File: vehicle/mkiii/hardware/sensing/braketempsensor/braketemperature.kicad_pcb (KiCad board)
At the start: 2 copper layers, 8.4 x 20.3 mm, 15 parts, among them J1 J_PCIe_x1, J2 J_Programming_Pin_Header, U1 MCP2561-E_SN, U2 STM32G441KBT6, Y1 X_16MHz_18pF

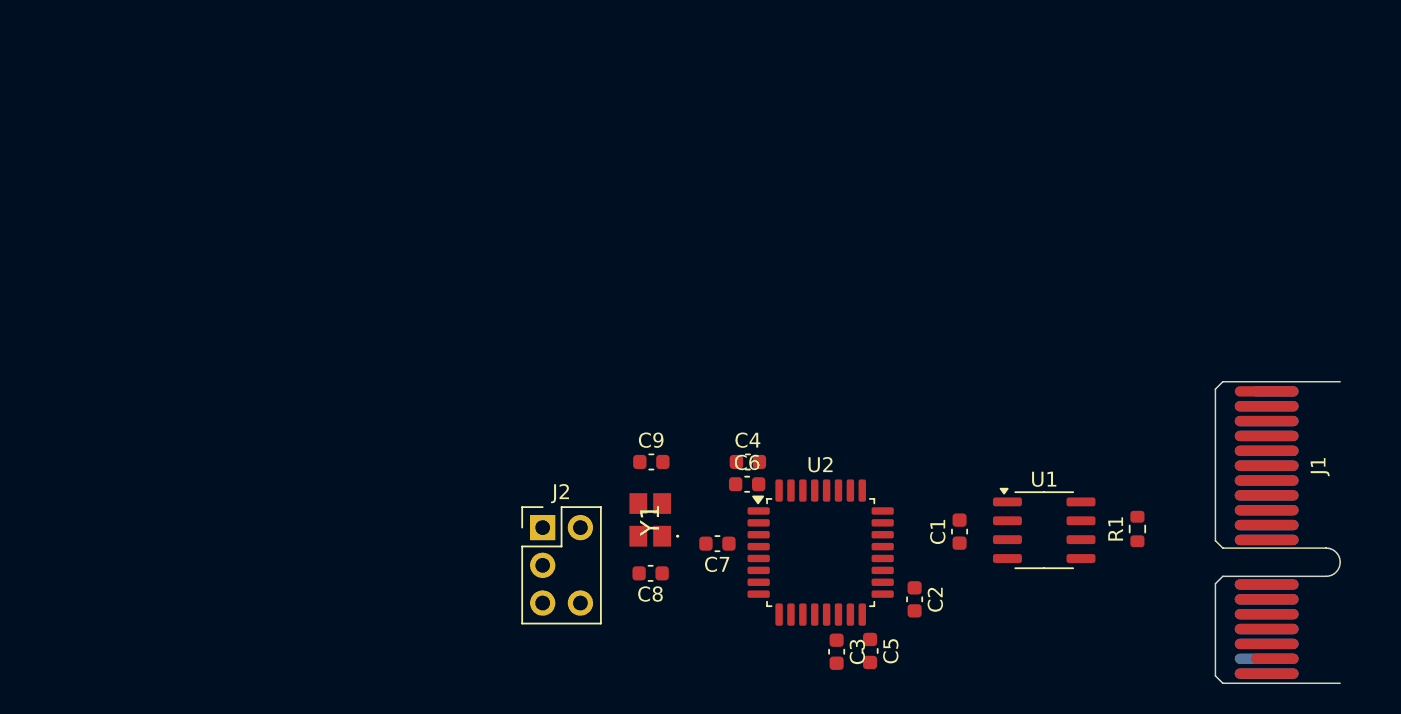
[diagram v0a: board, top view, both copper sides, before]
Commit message: first final draft of brake temp sensor, schematic and pcb layout first completion
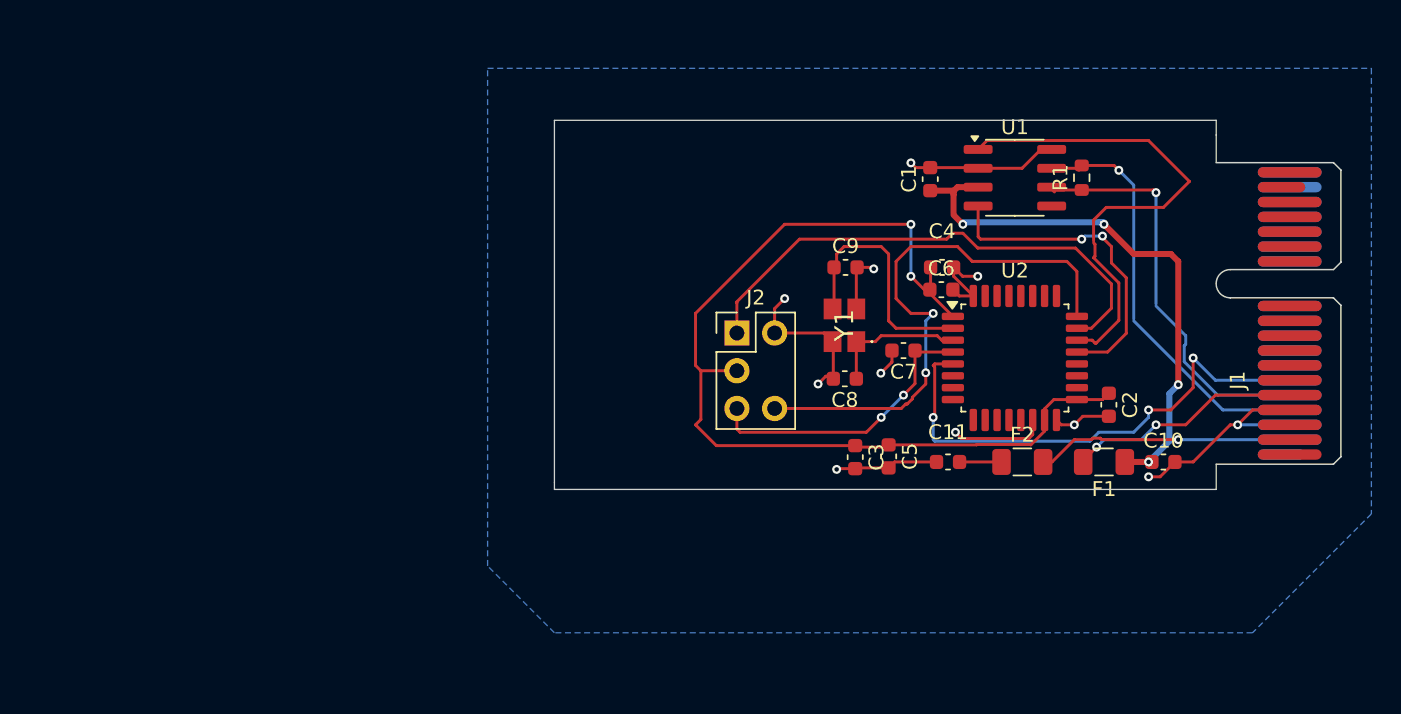
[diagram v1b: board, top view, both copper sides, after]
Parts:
- added C10: C_10uF_10V, OEM:C_0603_1608Metric, F.Cu at (270.0, 42.0)
- added C11: C_10uF_10V, OEM:C_0603_1608Metric, F.Cu at (255.5, 42.0)
- added F1: F_500mA_8V, OEM:Fuse_1206_3216Metric, F.Cu at (266.0, 42.0)
- added F2: F_500mA_8V, OEM:Fuse_1206_3216Metric, F.Cu at (260.5, 42.0)
- moved R1 23.9 mm to (264.5, 22.9)
- moved U1 23.8 mm to (260.0, 22.9)
- moved C1 23.8 mm to (254.3, 23.0)
- moved C6 18.5 mm to (255.1, 30.4)
- moved C8 18.5 mm to (248.6, 36.4)
- moved Y1 18.5 mm to (248.5, 32.8)
- moved C2 18.5 mm to (266.3, 38.1)
- moved C4 18.5 mm to (255.1, 28.9)
- moved C9 18.5 mm to (248.6, 28.9)
- moved J2 18.5 mm to (241.3, 33.3)
- moved U2 18.5 mm to (260.0, 35.0)
- moved C7 18.1 mm to (252.5, 34.5)
- moved C3 13.2 mm to (249.2, 41.7)
- moved C5 13.2 mm to (251.5, 41.6)
- moved J1 4.52 mm to (278.5, 41.5), turned to 90 degrees
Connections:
- J1 pad A2: +3.3V -> Net-(J1-3.3V)
- J1 pad B5: +5V -> Net-(J1-5V)
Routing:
- net +3V3: track 0.00 -> 67.2 mm, vias 0 -> 2
- net GND: track 0.00 -> 64.8 mm, vias 0 -> 11
- net +5V: track 0.00 -> 37.9 mm, vias 0 -> 4
- net /SWCLK: track 0.00 -> 37.6 mm, vias 0 -> 2
- net /SWDIO: track 0.00 -> 35.2 mm
- net /IR Output - PA0: track 0.00 -> 34.9 mm, vias 0 -> 3
- net /CAN_TX: track 0.00 -> 34.1 mm
- net Net-(J1-CAN+): track 0.00 -> 28.1 mm, vias 0 -> 1
- net Net-(J1-CAN-): track 0.00 -> 27.3 mm, vias 0 -> 1
- net /CAN_RX: track 0.00 -> 21.7 mm, vias 0 -> 2
- net /NRST: track 0.00 -> 19.7 mm, vias 0 -> 2
- net Net-(J1-3.3V): track 0.00 -> 17.3 mm, vias 0 -> 1
- net Net-(U2-PF0-OSC_IN): track 0.00 -> 16.5 mm
- net Net-(J1-5V): track 0.00 -> 16.3 mm, vias 0 -> 2
- net Net-(U2-PF1-OSC_OUT): track 0.00 -> 9.43 mm
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- added copper zone on B.Cu, net GND
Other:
- board size 8.4 x 20.3 mm -> 44.6 x 24.9 mm

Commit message: Fixed Vias DRC Issues by changing project to OEM Template
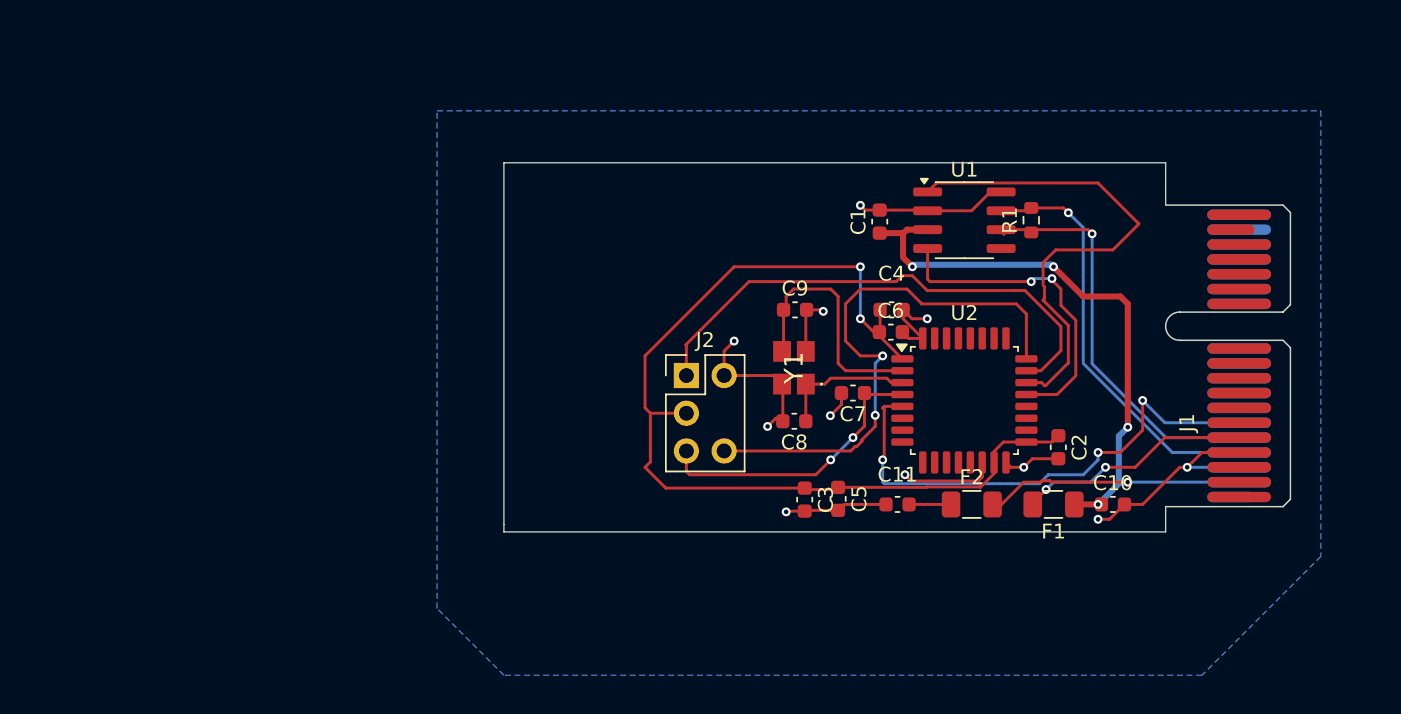
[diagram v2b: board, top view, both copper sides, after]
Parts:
- moved C4 4.44 mm to (251.7, 31.8)
- moved C9 4.44 mm to (245.2, 31.8)
- moved C1 4.44 mm to (250.9, 25.8)
- moved C11 4.44 mm to (252.1, 44.9)
- moved C3 4.44 mm to (245.8, 44.5)
- moved C5 4.44 mm to (248.1, 44.5)
- moved C6 4.44 mm to (251.7, 33.3)
- moved C7 4.44 mm to (249.1, 37.4)
- moved C8 4.44 mm to (245.2, 39.3)
- moved J2 4.44 mm to (237.9, 36.2)
- moved Y1 4.44 mm to (245.1, 35.7)
- moved R1 4.44 mm to (261.1, 25.7)
- moved U1 4.44 mm to (256.6, 25.7)
- moved C10 4.44 mm to (266.6, 44.9)
- moved C2 4.44 mm to (262.9, 41.0)
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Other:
- board size 44.6 x 24.9 mm -> 44.5 x 24.9 mm

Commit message: Brake Temp Sensor final version for review
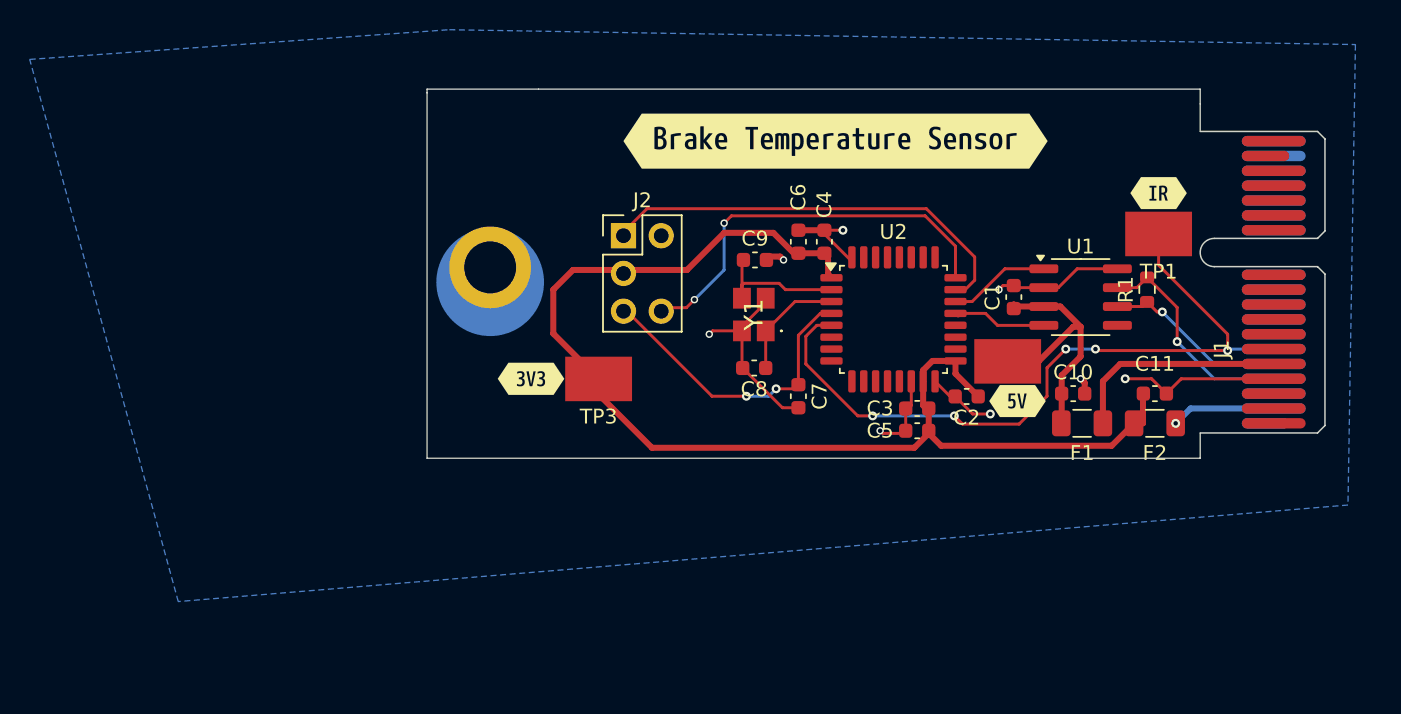
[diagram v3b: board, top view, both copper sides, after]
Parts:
- added H1: H_MountingHole, OEM:H_MountingHole, F.Cu at (224.7, 28.9)
- added TP1: TP_SMD, OEM:TP_Hook_SMD, F.Cu at (269.7, 26.6)
- added TP2: TP_SMD, OEM:TP_Hook_SMD, F.Cu at (259.5, 35.2)
- added TP3: TP_SMD, OEM:TP_Hook_SMD, F.Cu at (232.0, 36.4)
- added kibuzzard-697E6E94: G***, kibuzzard-697E6E94, F.Cu at (269.7, 23.9)
- added kibuzzard-697E6EEF: G***, kibuzzard-697E6EEF, F.Cu at (260.2, 37.9)
- added kibuzzard-697E6F70: G***, kibuzzard-697E6F70, F.Cu at (227.4, 36.4)
- added kibuzzard-697E6FE4: G***, kibuzzard-697E6FE4, F.Cu at (247.9, 20.4)
- moved C11 18.9 mm to (269.4, 37.4), turned to 0 degrees
- moved F2 13.5 mm to (269.4, 39.4)
- moved C1 10.4 mm to (259.9, 30.9)
- moved J2 10.3 mm to (233.7, 26.8)
- moved C3 9.75 mm to (253.4, 38.4), turned to 180 degrees
- moved U1 9.38 mm to (264.4, 30.9)
- moved R1 9.09 mm to (268.9, 30.4)
- moved C6 8.71 mm to (245.4, 27.2), turned to 90 degrees
- moved C10 7.93 mm to (263.9, 37.4)
- moved U2 7.25 mm to (251.8, 32.4)
- moved C2 7.05 mm to (256.8, 37.6), turned to 180 degrees
- moved C5 7.03 mm to (253.4, 39.9), turned to 180 degrees
- moved C4 6.44 mm to (247.2, 27.2), turned to 90 degrees
- moved F1 5.79 mm to (264.5, 39.4), turned to 0 degrees
- moved J1 5.48 mm to (277.4, 39.4)
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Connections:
- C11 pad 1: +3.3V -> +3V3
- F2 pad 1: +3.3V -> +3V3
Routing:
- net /CAN_TX: track 34.1 -> 6.86 mm
- net +5V: track 37.9 -> 18.3 mm, vias 4 -> 0
- net /IR Output - PA0: track 34.9 -> 51.1 mm, vias 3 -> 5
- net /CAN_RX: track 21.7 -> 6.54 mm, vias 2 -> 0
- net Net-(J1-CAN-): track 27.2 -> 12.4 mm
- net +3V3: track 67.2 -> 81.5 mm, vias 2 -> 0
- net GND: track 64.8 -> 50.7 mm, vias 11 -> 8
- net Net-(J1-CAN+): track 28.1 -> 15.0 mm
- net /SWCLK: track 37.6 -> 27.2 mm
- net Net-(J1-3.3V): track 17.3 -> 7.01 mm
- net Net-(U2-PF0-OSC_IN): track 16.5 -> 9.98 mm
- net /SWDIO: track 35.2 -> 29.0 mm
- net +3.3V: track 2.82 -> 0.00 mm
- net Net-(U2-PF1-OSC_OUT): track 9.43 -> 7.74 mm
- net Net-(J1-5V): track 16.3 -> 14.8 mm, vias 2 -> 0
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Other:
- board size 44.5 x 24.9 mm -> 52.1 x 24.9 mm

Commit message: Schematics and PCB Layout are Preliminarily Approved - DRC and ERC results are good.
Changes:
- Added Sensor Info to Schematics
- Updated Title Block in Schematics
- Added OEM Logo and Engineer's (Matthew T.) Name
- Moved Mounting Hole to Edge of PCB
- Shrank size of PCB by 4 mm

Good work Matthew :)
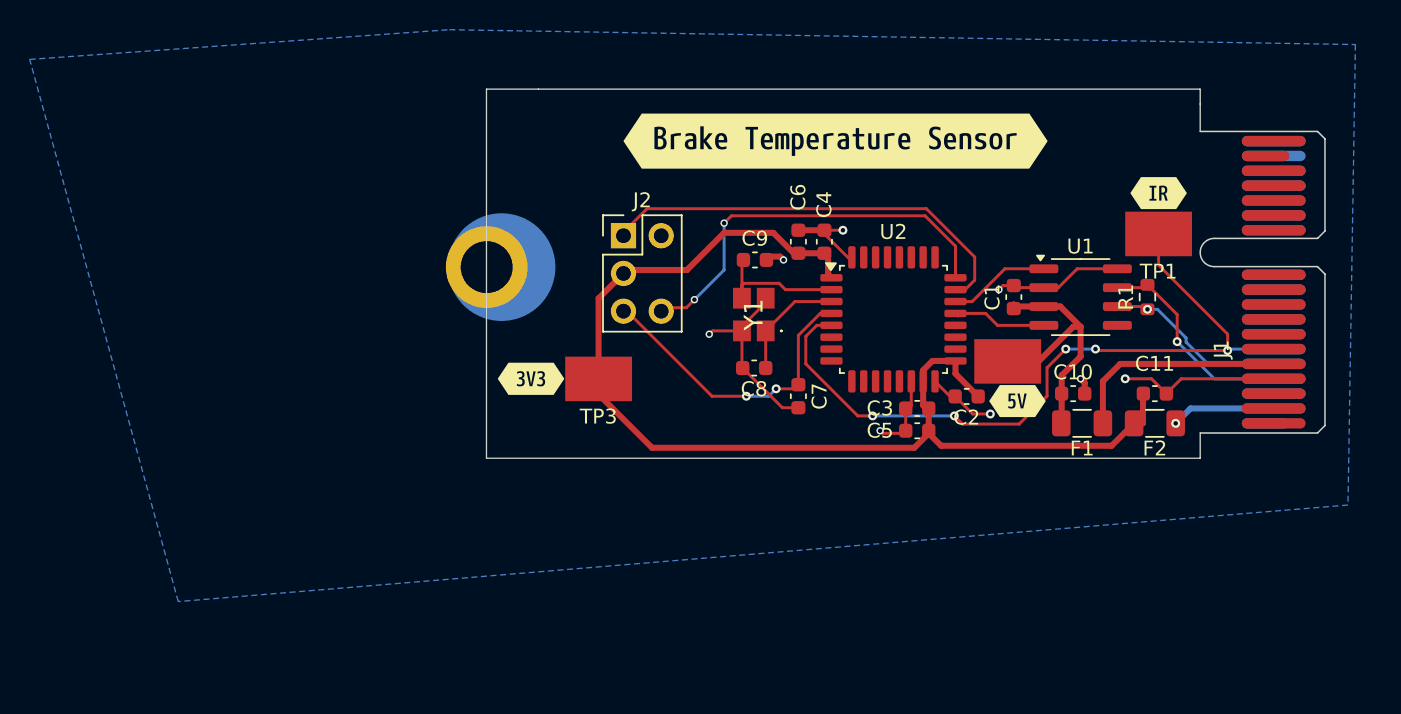
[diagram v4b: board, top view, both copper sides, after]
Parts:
- added REF**: OEM_Logo_8mm, OEM:OEM_Logo_8mm, B.Cu at (266.5, 22.9)
- added kibuzzard-697F802E: G***, kibuzzard-697F802E, B.Cu at (254.2, 22.9)
- added kibuzzard-697F80A9: G***, kibuzzard-697F80A9, B.Cu at (250.7, 20.1)
- added kibuzzard-697F80BA: G***, kibuzzard-697F80BA, B.Cu at (254.2, 25.7)
- moved R1 0.50 mm to (268.9, 30.9)
- moved H1 0.25 mm to (224.4, 28.9), turned to 90 degrees
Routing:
- net +3V3: track 81.5 -> 76.8 mm
- net Net-(J1-CAN+): track 15.0 -> 14.3 mm
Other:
- board size 52.1 x 24.9 mm -> 48.1 x 24.9 mm

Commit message: Brake temperature sensor final version 2/2/26
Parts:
- added D1: D_Red_LED, OEM:D_0805_2012Metric, F.Cu at (260.0, 39.2)
- added D2: D_Red_LED, OEM:D_0805_2012Metric, F.Cu at (226.8, 39.5)
- added D3: D_Red_LED, OEM:D_0805_2012Metric, F.Cu at (259.8, 25.5)
- added D4: D_Red_LED, OEM:D_0805_2012Metric, F.Cu at (241.8, 39.8)
- added D5: D_Red_LED, OEM:D_0805_2012Metric, F.Cu at (237.2, 37.5)
- added D6: D_Red_LED, OEM:D_0805_2012Metric, F.Cu at (235.8, 23.4)
- added R2: R_1k, OEM:R_0603_1608Metric, F.Cu at (259.8, 37.5)
- added R3: R_1k, OEM:R_0603_1608Metric, F.Cu at (228.5, 39.2)
- added R4: R_1k, OEM:R_0603_1608Metric, F.Cu at (258.0, 25.8)
- added R5: R_1k, OEM:R_0603_1608Metric, F.Cu at (247.2, 39.2)
- added R6: R_1k, OEM:R_0603_1608Metric, F.Cu at (235.2, 35.8)
- added R7: R_1k, OEM:R_0603_1608Metric, F.Cu at (233.0, 23.2)
- added TP4: TP_SMD, OEM:TP_Hook_SMD, F.Cu at (264.5, 19.8)
- added TP5: TP_SMD, OEM:TP_Hook_SMD, F.Cu at (264.5, 23.8)
- added TP6: TP_SMD, OEM:TP_Hook_SMD, F.Cu at (229.2, 24.5)
- added kibuzzard-69815F9D: G***, kibuzzard-69815F9D, F.Cu at (229.2, 21.6)
- added kibuzzard-69815FEC: G***, kibuzzard-69815FEC, F.Cu at (260.7, 19.6)
- added kibuzzard-69815FF8: G***, kibuzzard-69815FF8, F.Cu at (260.9, 23.0)
- added kibuzzard-69816079: G***, kibuzzard-69816079, F.Cu at (241.6, 38.2)
- added kibuzzard-69816083: G***, kibuzzard-69816083, F.Cu at (237.2, 34.3)
- added kibuzzard-69816091: G***, kibuzzard-69816091, F.Cu at (257.1, 23.5)
- moved kibuzzard-697E6EEF 4.91 mm to (264.1, 35.0)
- moved TP1 3.90 mm to (269.7, 22.8)
- moved kibuzzard-697E6E94 3.90 mm to (269.7, 20.0)
- moved kibuzzard-697E6FE4 3.05 mm to (245.0, 19.5)
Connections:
- U2 pad 11: unconnected-(U2-(TIM3_CH1/TIM16_CH1/GPIO_EXTI6/ADC2_IN3)PA6*-Pad11) -> /Debug LED
- U2 pad 18: unconnected-(U2-(TIM4_ETR/USART1_CK/GPIO_EXTI8)PA8-Pad18) -> /Heartbeat LED
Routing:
- net Net-(J1-CAN+): track 14.3 -> 27.4 mm
- net GND: track 50.7 -> 62.5 mm, vias 8 -> 13
- net Net-(J1-CAN-): track 12.3 -> 22.6 mm, vias 1 -> 2
- net /Heartbeat LED: track 0.00 -> 9.27 mm, vias 0 -> 2
- net /IR Output - PA0: track 51.1 -> 57.1 mm
- net /Debug LED: track 0.00 -> 4.75 mm, vias 0 -> 2
- net Net-(D4-A): track 0.00 -> 4.70 mm
- net +3V3: track 76.8 -> 81.4 mm
- net +5V: track 18.3 -> 22.3 mm
- net /SWDIO: track 29.0 -> 31.7 mm
- net Net-(D5-A): track 0.00 -> 2.25 mm
- net Net-(D6-A): track 0.00 -> 2.21 mm
- net Net-(D1-A): track 0.00 -> 1.90 mm
- net Net-(D3-A): track 0.00 -> 1.90 mm
- net Net-(D2-A): track 0.00 -> 1.90 mm
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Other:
- outline, holes or cut-outs redrawn
- board text added: "Mascot"

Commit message: Added Subteam Logo and Production Files
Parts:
- added G***: LOGO, LOGO, B.Cu at (248.8, 34.8)
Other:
- board text removed: "Mascot"
